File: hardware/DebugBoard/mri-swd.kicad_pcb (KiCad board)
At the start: 2 copper layers, 41.7 x 68.6 mm, 11 parts, among them J1 Debug UART/Power, J2 Debug SWD, J5 OLED, SW1 Reset, SW2 Halt on Connect, U1 PicoW

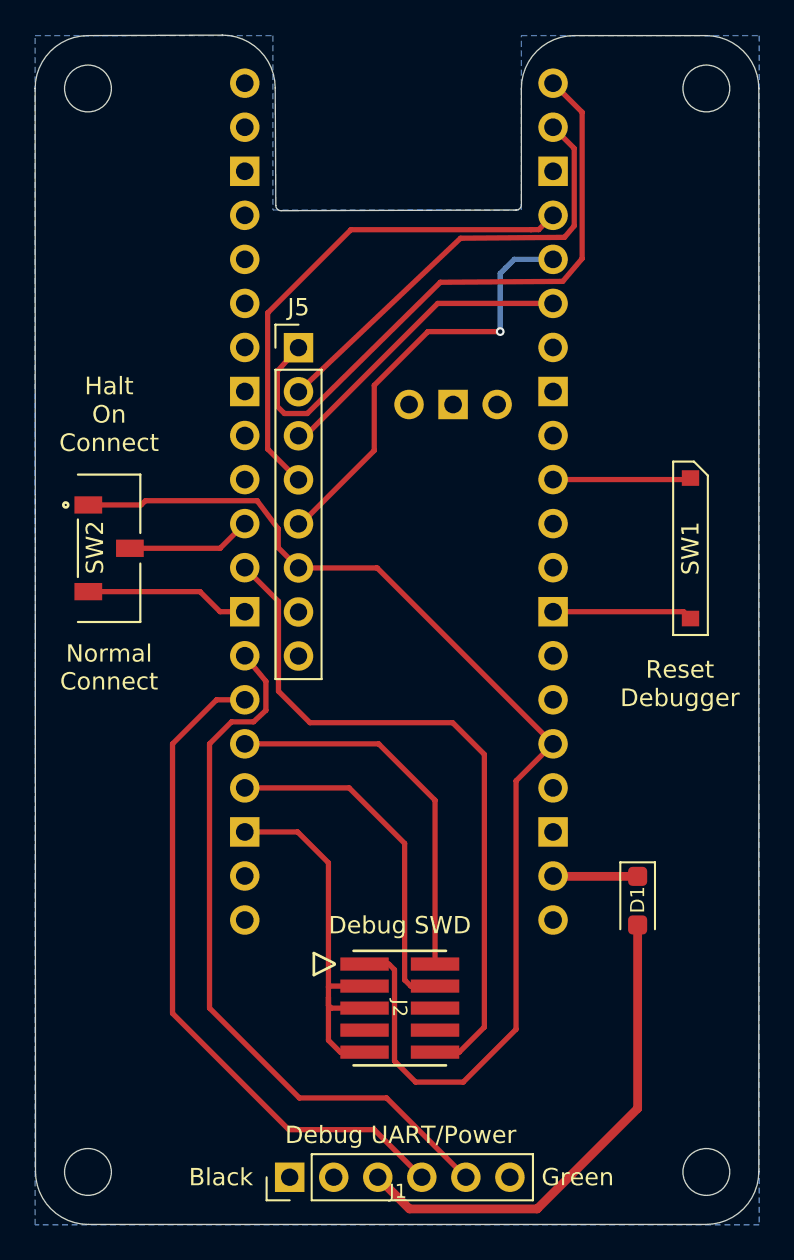
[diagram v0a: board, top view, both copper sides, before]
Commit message: Fixes to PCB found during Chomps bring up
I hit a few issues when attempting to use the mri-swd DebugBoard PCB
with the initial revision of my Chomps main board:
* The VTref pin of the SWD connector was connected to 3.3V on the debug
  board. This meant that both the target and the debugger were applying
  power to this bus. I now have the VTref pin of the SWD connector left
  unconnected. I hacked the same change into my already manufactured
  PCBs by cutting the trace leading away from the VTref pin.
* The nReset pin of the SWD connector is connected to the GPIO6 pin of
  the Pico with nothing else. This meant that nReset was connected to
  ground via the default ~50kohm pulldown of the debugger's RP2040
  and also pulled up by the default ~50kohm pull-up of the target's
  RP2040 so the voltage sits pretty close to the transition area which
  causes very weird behavior in the target and the debugger fails to
  successfully connect to the target via SWD. I added an external
  1kohm pull-up resistor to the debugger board to override the
  default pulldown behavior of the RP2040. I hacked the same change into
  my already manufactured PCBs by bodging in a 1kohm through hole
  resistor between the Pico's GPIO6 and 3.3V pins.

I bumped the version of the schematic and PCB up to 1.1 after these
changes were applied.
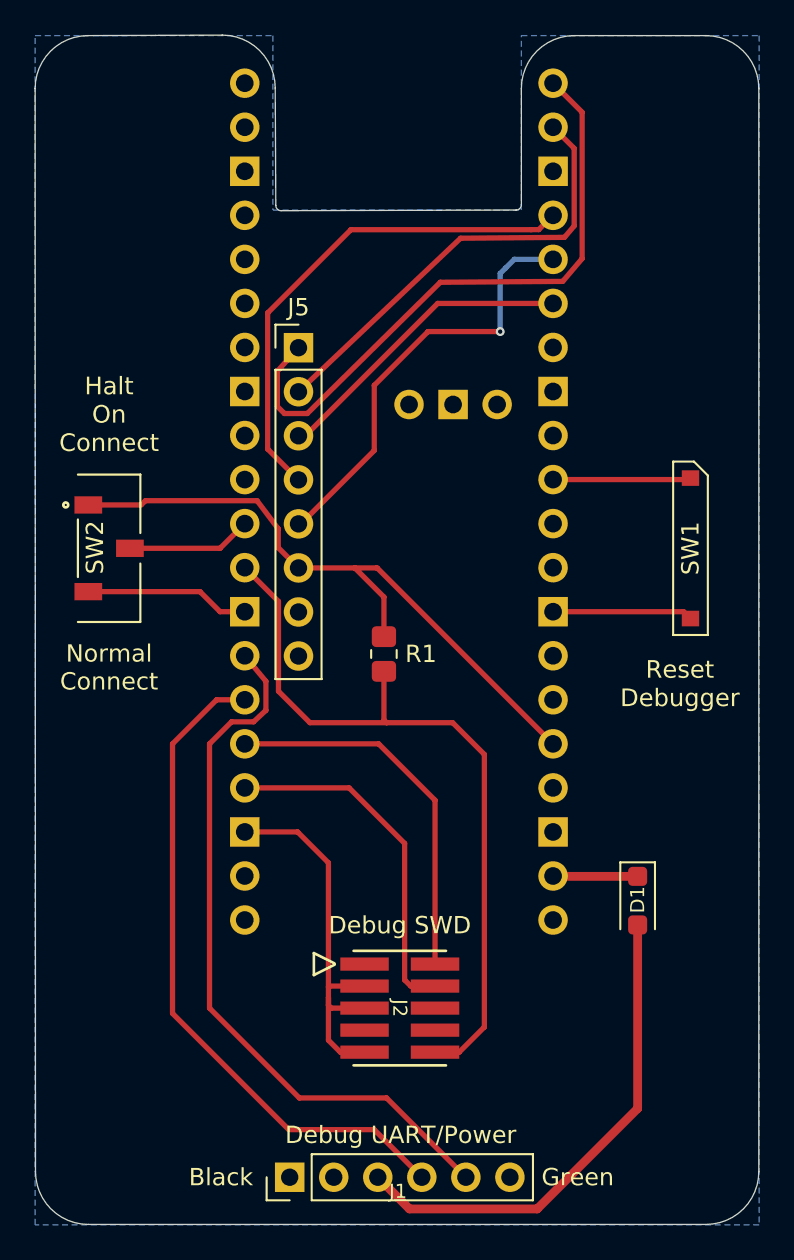
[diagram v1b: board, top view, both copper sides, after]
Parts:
- removed REF** (x4): MountingHole_2.7mm_M2.5, MountingHole:MountingHole_2.7mm_M2.5
- added R1: 1kΩ, Resistor_SMD:R_0805_2012Metric_Pad1.20x1.40mm_HandSolder, F.Cu at (125.0, 97.8)
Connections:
- J2 pad 1: +3.3V -> unconnected-(J2-VTref-Pad1)
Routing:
- net +3.3V: track 66.7 -> 38.1 mm
- net /SWD_RESET: track 40.5 -> 43.5 mm
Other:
- board text added: "https://github.com/adamgreen/mri-swd v1.1"
- board text removed: "https://github.com/adamgreen/mri-swd v1.0"

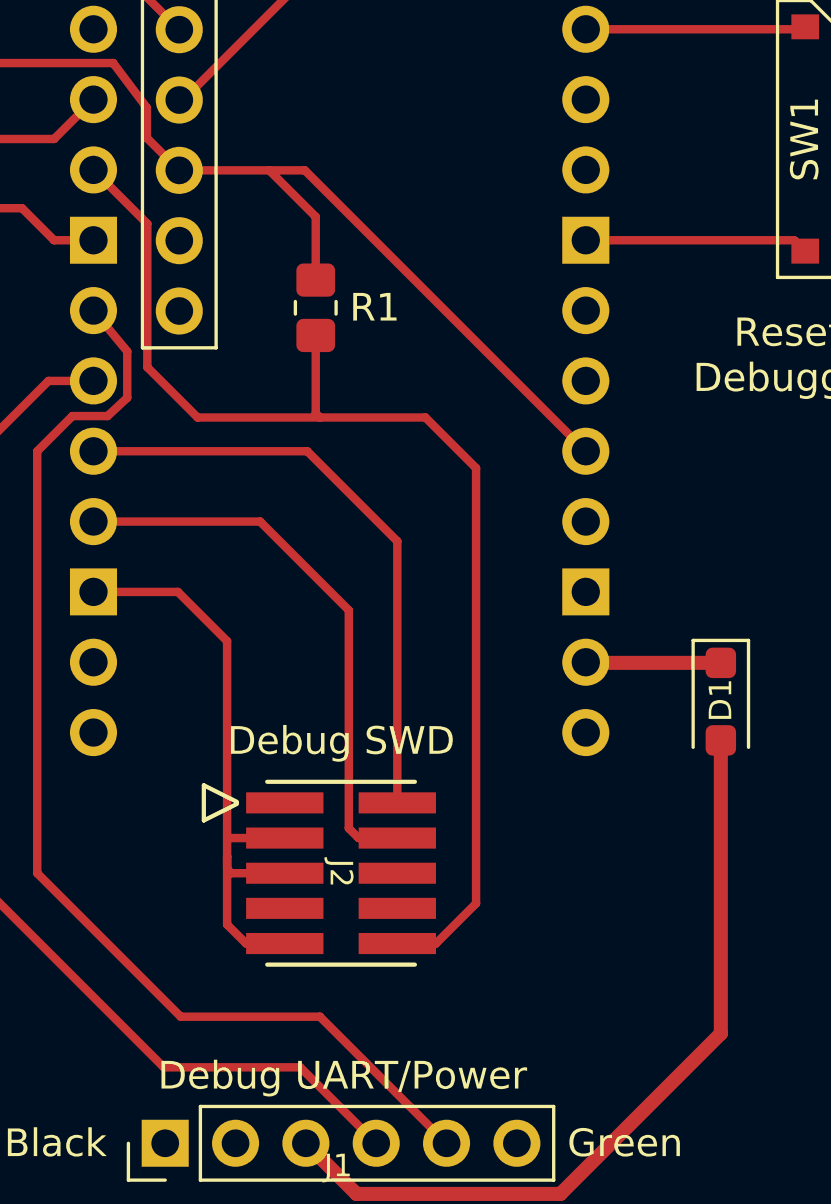
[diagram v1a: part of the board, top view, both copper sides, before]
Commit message: More fixes to PCB found during Chomps bring up
I hit another issue when attempting to use the mri-swd DebugBoard PCB
with the initial revision of my Chomps main board:
* I previously added a 1kohm pull-up resistor to the nReset pin on the
  SWD connector but I connected it to the regulated 3.3V on the
  debugger board rather than the VTref pin on the SWD connector. This
  means that nReset wasn't pulled-up correctly if the debugger board
  wasn't powered up. Now it does the right thing even if the debugger
  board is connected to a target but hasn't been yet powered up.

I bumped the version of the schematic and PCB up to 1.2 after these
changes were applied.
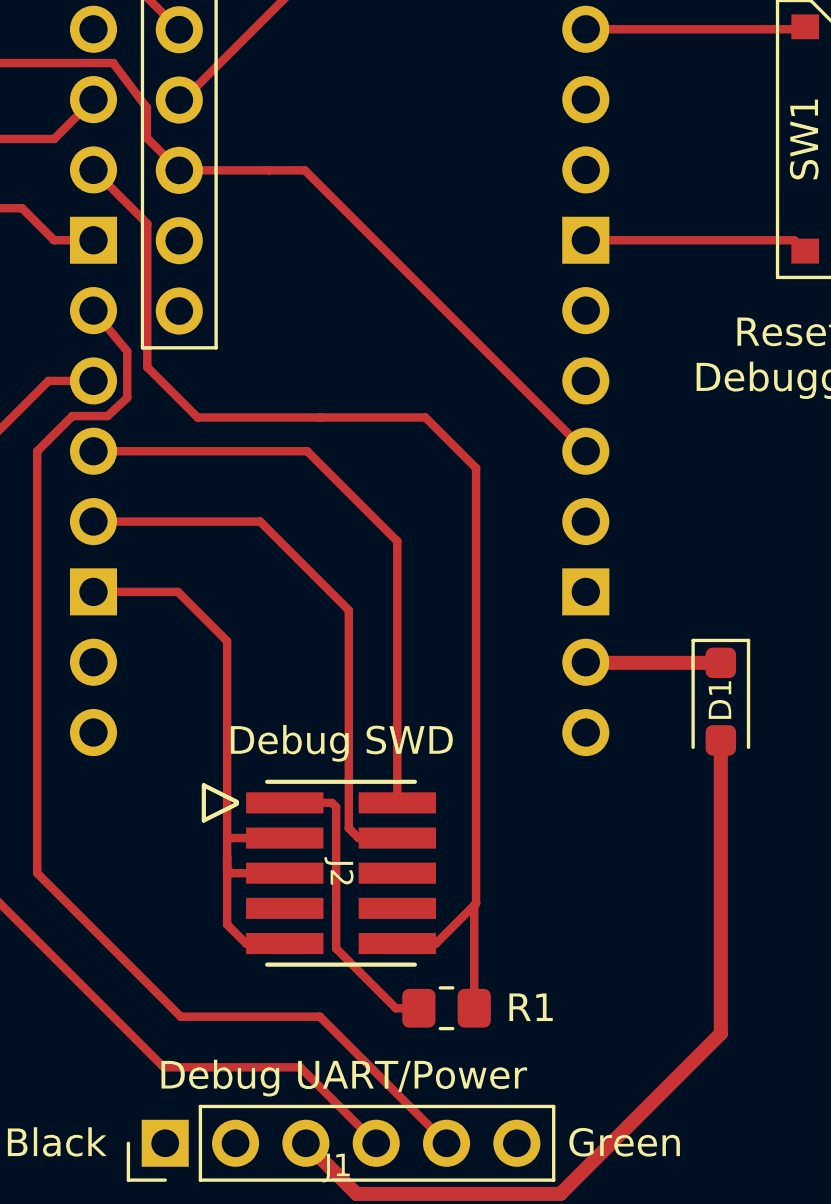
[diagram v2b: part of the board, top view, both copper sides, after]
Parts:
- moved R1 25.7 mm to (129.7, 123.1), turned to 0 degrees
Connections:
- J2 pad 1: unconnected-(J2-VTref-Pad1) -> Net-(J2-VTref)
- R1 pad 1: +3.3V -> Net-(J2-VTref)
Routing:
- net Net-(J2-VTref): track 0.00 -> 10.9 mm
- net +3.3V: track 38.1 -> 33.5 mm
- net /SWD_RESET: track 43.5 -> 44.3 mm
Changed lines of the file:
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@@
 	(paper "A4")
 	(title_block
-		(date "2024-07-13")
+		(date "2024-07-28")
 		(rev "1.1")
 	)
@@
 			(sketchpadsonfab no)
 			(subtractmaskfromsilk no)
-			(outputformat 1)
+			(outputformat 4)
 			(mirror no)
-			(drillshape 1)
+			(drillshape 0)
 			(scaleselection 1)
 			(outputdirectory "")
@@
 	(net 41 "unconnected-(U1-SWDIO-Pad43)")
 	(net 42 "unconnected-(U1-GPIO21-Pad27)")
-	(net 43 "unconnected-(J2-VTref-Pad1)")
+	(net 43 "Net-(J2-VTref)")
 	(footprint "Connector_PinHeader_2.54mm:PinHeader_1x08_P2.54mm_Vertical"
 		(layer "F.Cu")
@@
 	(footprint "Resistor_SMD:R_0805_2012Metric_Pad1.20x1.40mm_HandSolder"
 		(layer "F.Cu")
-		(at 124.968 97.8408 -90)
+		(at 129.6924 123.1392)
 		(descr "Resistor SMD 0805 (2012 Metric), square (rectangular) end terminal, IPC_7351 nominal with elongated pad for handsoldering. (Body size source: IPC-SM-782 page 72, https://www.pcb-3d.com/wordpress/wp-content/uploads/ipc-sm-782a_amendment_1_and_2.pdf), generated with kicad-footprint-generator")
 		(tags "resistor handsolder")
 		(property "Reference" "R1"
-			(at 0 -2.1336 180)
+			(at 3.048 0 180)
 			(layer "F.SilkS")
 			(effects
@@
 		)
 		(property "Value" "1kΩ"
-			(at 0 1.65 90)
+			(at -3.6576 0 360)
 			(layer "F.Fab")
 			(effects
@@
 		)
 		(property "Footprint" "Resistor_SMD:R_0805_2012Metric_Pad1.20x1.40mm_HandSolder"
-			(at 0 0 -90)
+			(at 0 0 0)
 			(unlocked yes)
 			(layer "F.Fab")
@@
 		)
 		(property "Datasheet" ""
-			(at 0 0 -90)
+			(at 0 0 0)
 			(unlocked yes)
 			(layer "F.Fab")
@@
 		)
 		(property "Description" "Resistor, US symbol"
-			(at 0 0 -90)
+			(at 0 0 0)
 			(unlocked yes)
 			(layer "F.Fab")
@@
 		(attr smd)
 		(fp_line
-			(start -0.227064 0.735)
-			(end 0.227064 0.735)
+			(start -0.227064 -0.735)
+			(end 0.227064 -0.735)
 			(stroke
 				(width 0.12)
@@
 		)
 		(fp_line
-			(start -0.227064 -0.735)
-			(end 0.227064 -0.735)
+			(start -0.227064 0.735)
+			(end 0.227064 0.735)
 			(stroke
 				(width 0.12)
@@
 		)
 		(fp_line
-			(start -1.85 0.95)
-			(end -1.85 -0.95)
+			(start -1.85 -0.95)
+			(end 1.85 -0.95)
 			(stroke
 				(width 0.05)
@@
 		)
 		(fp_line
-			(start 1.85 0.95)
-			(end -1.85 0.95)
+			(start -1.85 0.95)
+			(end -1.85 -0.95)
 			(stroke
 				(width 0.05)
@@
 		)
 		(fp_line
-			(start -1.85 -0.95)
-			(end 1.85 -0.95)
+			(start 1.85 -0.95)
+			(end 1.85 0.95)
 			(stroke
 				(width 0.05)
@@
 		)
 		(fp_line
-			(start 1.85 -0.95)
-			(end 1.85 0.95)
+			(start 1.85 0.95)
+			(end -1.85 0.95)
 			(stroke
 				(width 0.05)
@@
 		)
 		(fp_line
-			(start -1 0.625)
-			(end -1 -0.625)
+			(start -1 -0.625)
+			(end 1 -0.625)
 			(stroke
 				(width 0.1)
@@
 		)
 		(fp_line
-			(start 1 0.625)
-			(end -1 0.625)
+			(start -1 0.625)
+			(end -1 -0.625)
 			(stroke
 				(width 0.1)
@@
 		)
 		(fp_line
-			(start -1 -0.625)
-			(end 1 -0.625)
+			(start 1 -0.625)
+			(end 1 0.625)
 			(stroke
 				(width 0.1)
@@
 		)
 		(fp_line
-			(start 1 -0.625)
-			(end 1 0.625)
+			(start 1 0.625)
+			(end -1 0.625)
 			(stroke
 				(width 0.1)
@@
 		)
 		(fp_text user "${REFERENCE}"
-			(at 0 0 90)
+			(at 0 0 360)
 			(layer "F.Fab")
 			(effects
@@
 		)
 		(pad "1" smd roundrect
-			(at -1 0 270)
+			(at -1 0)
 			(size 1.2 1.4)
 			(layers "F.Cu" "F.Paste" "F.Mask")
 			(roundrect_rratio 0.208333)
-			(net 8 "+3.3V")
+			(net 43 "Net-(J2-VTref)")
 			(pintype "passive")
 		)
 		(pad "2" smd roundrect
-			(at 1 0 270)
+			(at 1 0)
 			(size 1.2 1.4)
 			(layers "F.Cu" "F.Paste" "F.Mask")
@@
 			(size 0.762 2.794)
 			(layers "F.Cu" "F.Paste" "F.Mask")
-			(net 43 "unconnected-(J2-VTref-Pad1)")
+			(net 43 "Net-(J2-VTref)")
 			(pinfunction "VTref")
-			(pintype "power_in+no_connect")
+			(pintype "power_in")
 		)
 		(pad "2" smd rect
@@
 	)
 	(segment
-		(start 124.968 96.8408)
-		(end 124.968 94.5538)
-		(width 0.3048)
-		(layer "F.Cu")
-		(net 8)
-	)
-	(segment
-		(start 124.968 94.5538)
-		(end 123.2916 92.8774)
-		(width 0.3048)
-		(layer "F.Cu")
-		(net 8)
-	)
-	(segment
 		(start 124.555558 92.8774)
 		(end 123.2916 92.8774)
@@
 	)
 	(segment
-		(start 124.968 98.8408)
-		(end 124.968 101.6508)
+		(start 130.6924 119.4214)
+		(end 130.7592 119.3546)
 		(width 0.3048)
 		(layer "F.Cu")
@@
 	)
 	(segment
-		(start 118.8856 94.8064)
-		(end 118.8856 99.988)
+		(start 130.6924 123.1392)
+		(end 130.6924 119.4214)
 		(width 0.3048)
 		(layer "F.Cu")
@@
 	)
 	(segment
-		(start 120.7008 101.8032)
-		(end 125.1204 101.8032)
+		(start 118.8856 94.8064)
+		(end 118.8856 99.988)
 		(width 0.3048)
 		(layer "F.Cu")
@@
 	)
 	(segment
-		(start 124.968 101.6508)
+		(start 120.7008 101.8032)
 		(end 125.1204 101.8032)
 		(width 0.3048)
@@
 		(net 22)
 	)
+	(segment
+		(start 125.5522 115.7224)
+		(end 125.7046 115.8748)
+		(width 0.3048)
+		(layer "F.Cu")
+		(net 43)
+	)
+	(segment
+		(start 125.7046 115.8748)
+		(end 125.7046 120.9802)
+		(width 0.3048)
+		(layer "F.Cu")
+		(net 43)
+	)
+	(segment
+		(start 127.8636 123.1392)
+		(end 128.6924 123.1392)
+		(width 0.3048)
+		(layer "F.Cu")
+		(net 43)
+	)
+	(segment
+		(start 123.8504 115.7224)
+		(end 125.5522 115.7224)
+		(width 0.3048)
+		(layer "F.Cu")
+		(net 43)
+	)
+	(segment
+		(start 125.7046 120.9802)
+		(end 127.8636 123.1392)
+		(width 0.3048)
+		(layer "F.Cu")
+		(net 43)
+	)
 	(zone
